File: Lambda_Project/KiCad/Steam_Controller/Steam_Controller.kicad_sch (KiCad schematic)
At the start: 156 parts, among them J1 MICROQTJ, P1 Conn_ARM_SWD_TagConnect_TC2030, P2 Conn_ARM_SWD_TagConnect_TC2030, P3 781271220, P4 781271220, Q10 DMN2300U-7, Q11 DMN2300U-7, Q12 DMP2035U-7, Q2 DMP2035U-7, Q3 MMBT3906, Q4 DMP2035U-7, Q5 DMP2035U-7, Q6 FDV304P, Q8 FDV304P, U1 LPC11U37FBD64/501,, U10 DMN63D8LDW-7, U2 TPD4E1U06DBVR - NG4P USB, U3 TPS61029DRCR, U4 TLV70230DBVT, U5 NRF51822-QFAB-T, U6 MPU6500, U7 A1304ELHLT-T, U8 A1304ELHLT-T, U9 DMN63D8LDW-7, X1 ABM8G-12.000MHZ-18-D2Y-T, X2 NX2520SA-16MHZ-STD-CSW-5

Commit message: Updated TODO in Schematic
Added a new TODO objective in the schematic as a test for the discord bot
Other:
- note added: "TODO: While tracing, keep an eye on the schematic and make sure it is correctt"
- note removed: "TODO: Sanity Check, reference datasheets, measure unsure values again."
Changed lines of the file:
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@@
 		)
 	)
-	(text "TODO: Sanity Check, reference datasheets, measure unsure values again."
+	(text "TODO: While tracing, keep an eye on the schematic and make sure it is correctt"
 		(exclude_from_sim no)
 		(at 513.334 51.562 0)
@@
 	)
 	(label "Inductor & Capacitor values taken from datasheet. These need to be high tolerance, within 1%"
-		(at 116.84 218.44 0)
+		(at 116.84 217.17 0)
 		(effects
 			(font

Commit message: V0.99 Update
Added trace updates from RoyMeetsWorld. Updated README. Added new images. Cleaned up some of the schematic and pcb.
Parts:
- added TP1, TP10, TP11, TP12, TP13, TP14, TP15, TP16, TP17, TP18, TP19, TP2, TP20, TP21, TP22, TP23, TP24, TP25, TP26, TP27, TP28, TP29, TP3, TP30, TP31, TP32, TP33, TP34, TP35, TP36, TP37, TP38, TP39, TP4, TP40, TP41, TP42, TP43, TP44, TP45, TP46, TP47, TP48, TP49, TP5, TP50, TP51, TP52, TP6, TP7, TP8, TP9: TestPoint, Steam_Controller:Steam Controller Test Pad, symbol Connector:TestPoint
- X1: value ABM8G-12.000MHZ-18-D2Y-T -> ABM8-12.000MHZ-B2-T
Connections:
- net A: now also TP17.1
- net ATP6 Left Signal: now also TP43.1
- net ATP6 Right Signal: now also TP8.1
- net B: now also TP12.1
- net D+: no longer J1.3 (D+)
- net D-: no longer J1.2 (D-)
- net FL: now also TP46.1
- net FR: now also TP51.1
- net GND: now also E1.1 (ANT1), TP10.1, TP24.1, TP48.1; no longer E1.2 (ANT2)
- net HALLTRIG1: now also TP31.1
- net HALLTRIG2: now also TP5.1
- net JOYBTN: now also TP26.1
- net JOYX: now also TP40.1
- net JOYY: now also TP41.1
- net LB: now also TP32.1
- net LED: now also TP47.1
- net LED Cathode: now also TP45.1
- net LT: now also TP30.1
- net RB: now also TP4.1
- net RT: now also TP6.1
- net S14: now also TP27.1
- net S16: now also TP11.1
- net S5: now also TP7.1
- net STEAM: now also TP36.1
- net U1-62: now also TP42.1
- net VBUS: now also TP1.1
- net VDD: now also TP23.1, TP28.1
- net X: now also TP16.1
- net Y: now also TP18.1
- net Net-(U1-PIO1_8): now reaches R39.2, R45.2, U1.36 (PIO0_8)
- net Net-(U1-PIO1_8): now also TP39.1
- net Net-(LED-C): now reaches LED1.1 (C), R1.1
- net Net-(LED-C): now also TP44.1
- net Net-(Bat1-Pos): now reaches BAT1.1 (pos), C57.1, D1.2 (A), D6.1 (K), Q4.2 (S)
- net Net-(Bat1-Pos): now also TP52.1
- net D+ USB: now reaches R14.1, R15.1, U2.1 (D1+)
- net D+ USB: now also J1.3 (D+), TP2.1
- net D3-K: now reaches C20.1, C22.2, C46.2, D3.1 (K), L1.1, Q12.2 (S), U3.1 (EN), U3.6 (VBAT)
- net D3-K: now also TP29.1
- net Net-(U1-PIO0_5): now reaches R7.2, U1.21 (PIO0_5), U6.24 (SDA/SDI)
- net Net-(U1-PIO0_5): now also TP35.1
- net Net-(U1-PIO1_17): now reaches U1.23 (PIO1_17), U5.20 (P0.14)
- net Net-(U1-PIO1_17): now also TP19.1
- net Net-(U1-PIO1_18): now reaches U1.28 (PIO1_18), U5.21 (P0.15)
- net Net-(U1-PIO1_18): now also TP20.1
- net Net-(U1-PIO1_9): now reaches R40.2, R46.1, U1.37 (PIO0_9)
- net Net-(U1-PIO1_9): now also TP38.1
- net P1-RESET: now reaches P1.3 (~{RESET}), R23.1
- net P1-RESET: now also TP15.1
- net Net-(U1-PIO1_29): now reaches R37.2, R41.1, U1.41 (PIO1_29)
- net Net-(U1-PIO1_29): now also TP37.1
- net P3-SS: now reaches P3.10 (SS), U1.64 (PIO1_6)
- net P3-SS: now also TP21.1
- net P3-ATP4: now reaches P3.5 (GND/ATP4)
- net P3-ATP4: now also TP25.1
- net P3-DR: now reaches P3.9 (DR), U1.63 (PIO1_16)
- net P3-DR: now also TP22.1
- net at C50.1, R44.2: now also E1.2 (ANT2); no longer E1.1 (ANT1)
- net Net-(U1-PIO0_4): now reaches R6.2, U1.20 (PIO0_4), U6.23 (SCL/SCLK)
- net Net-(U1-PIO0_4): now also TP34.1
- net Net-(U1-PIO1_23): now reaches U1.24 (PIO1_23), U6.12 (INT)
- net Net-(U1-PIO1_23): now also TP33.1
- net Net-(U1-PIO1_7): now reaches U1.30 (PIO0_7)
- net Net-(U1-PIO1_7): now also TP49.1
- net Net-(U1-PIO1_28): now reaches U1.31 (PIO1_28)
- net Net-(U1-PIO1_28): now also TP50.1
- net P4-DR: now reaches P4.9 (DR), U1.56 (PIO0_23)
- net P4-DR: now also TP13.1
- net P4-SS: now reaches P4.10 (SS), U1.57 (PIO1_15)
- net P4-SS: now also TP14.1
- net D- USB: now reaches R16.2, U2.6 (D1-)
- net D- USB: now also J1.2 (D-), TP3.1
- net P4-ATP4: now reaches P4.5 (GND/ATP4)
- net P4-ATP4: now also TP9.1
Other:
- note removed: "Front Left"
- note removed: "TODO: While tracing, keep an eye on the schematic and make sure it is correctt"
- moved on the sheet: E1

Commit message: Replaced MCU-6500 with BMI270 dual gyro
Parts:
- removed C35: 100nF, Capacitor_SMD:C_0201_0603Metric, symbol Device:C
- removed R6, R7: 4.7kΩ, Resistor_SMD:R_0201_0603Metric, symbol Device:R_US
- removed U6: MPU6500, Steam_Controller:QFN-24_L3.0-W3.0-P0.40-BL-EP, symbol Steam_Controller_Symbols:MPU6500
- added C21: 10nF, Capacitor_SMD:C_0201_0603Metric, symbol Device:C
- added C31, C7: 100nF, Capacitor_SMD:C_0201_0603Metric, symbol Device:C
- added R2, R5: 4.7kΩ, Resistor_SMD:R_0201_0603Metric, symbol Device:R_US
- added U11, U6: BMI270, Steam_Controller:XDCR_BMI270, symbol Steam_Controller_Symbols:BMI270
- C37: value 10nF -> 100nF
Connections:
- net Net-(U1-PIO1_23) is gone; now on net Net-(U1-PIO1_17): TP33.1, U1.24 (PIO1_23)
- net Net-(U1-PIO1_9) is gone; now on net Net-(U1-PIO1_8): R40.2, R46.1, TP38.1, U1.37 (PIO0_9)
- net GND: now also C36.1, C37.1, C21.2, C31.1, C7.1, U11.6 (GNDIO), U11.7 (GND), U6.1 (SDO), U6.6 (GNDIO), U6.7 (GND); no longer C36.2, C37.2
- net Net-(U1-PIO0_4): now also R2.1, U11.13 (SCX), U6.13 (SCX)
- net Net-(U1-PIO0_5): now also R5.1, U11.14 (SDX), U6.14 (SDX)
- net Net-(U1-PIO1_17): now also U11.4 (INT1)
- net VDD: now also C36.2, C37.2, C21.1, C31.2, C7.2, R2.2, R5.2, U11.1 (SDO), U11.5 (VDDIO), U11.8 (VDD), U6.5 (VDDIO), U6.8 (VDD); no longer C37.1
- net at U1.53 (PIO0_16): now also U6.4 (INT1)

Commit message: Fix overlapping routing of INT trace to U11
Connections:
- net Net-(U1-PIO1_17): no longer TP33.1, U1.24 (PIO1_23), U11.4 (INT1)
- new net Net-(U1-PIO1_23): TP33.1, U1.24 (PIO1_23), U11.4 (INT1)
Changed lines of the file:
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@@
 	)
 	(junction
-		(at 205.74 185.42)
-		(diameter 0)
-		(color 0 0 0 0)
-	)
-	(junction
 		(at 353.06 23.368)
 		(diameter 0)
@@
 	)
 	(junction
+		(at 269.24 158.75)
+		(diameter 0)
+		(color 0 0 0 0)
+	)
+	(junction
 		(at 307.34 10.16)
 		(diameter 0)
@@
 	)
 	(junction
-		(at 262.89 185.42)
-		(diameter 0)
-		(color 0 0 0 0)
-	)
-	(junction
 		(at 293.37 332.74)
 		(diameter 0)
@@
 	(wire
 		(pts
-			(xy 262.89 185.42) (xy 497.84 185.42)
-		)
-		(stroke
-			(width 0)
-			(type default)
-		)
-	)
-	(wire
-		(pts
 			(xy 375.92 25.908) (xy 375.92 27.94)
 		)
@@
 	(wire
 		(pts
-			(xy 205.74 158.75) (xy 279.4 158.75)
-		)
-		(stroke
-			(width 0)
-			(type default)
-		)
-	)
-	(wire
-		(pts
 			(xy 267.97 335.28) (xy 267.97 342.9)
 		)
@@
 	(wire
 		(pts
-			(xy 262.89 185.42) (xy 205.74 185.42)
+			(xy 66.04 185.42) (xy 262.89 185.42)
 		)
 		(stroke
@@
 	(wire
 		(pts
+			(xy 260.35 158.75) (xy 269.24 158.75)
+		)
+		(stroke
+			(width 0)
+			(type default)
+		)
+	)
+	(wire
+		(pts
 			(xy 123.19 142.24) (xy 123.19 110.49)
 		)
@@
 	(wire
 		(pts
+			(xy 269.24 185.42) (xy 497.84 185.42)
+		)
+		(stroke
+			(width 0)
+			(type default)
+		)
+	)
+	(wire
+		(pts
 			(xy 233.68 394.97) (xy 247.65 394.97)
 		)
@@
 	(wire
 		(pts
+			(xy 269.24 158.75) (xy 279.4 158.75)
+		)
+		(stroke
+			(width 0)
+			(type default)
+		)
+	)
+	(wire
+		(pts
 			(xy 347.98 120.65) (xy 342.9 120.65)
 		)
@@
 	(wire
 		(pts
+			(xy 269.24 158.75) (xy 269.24 185.42)
+		)
+		(stroke
+			(width 0)
+			(type default)
+		)
+	)
+	(wire
+		(pts
 			(xy 72.39 168.91) (xy 67.31 168.91)
 		)
@@
 	(wire
 		(pts
-			(xy 205.74 158.75) (xy 205.74 185.42)
-		)
-		(stroke
-			(width 0)
-			(type default)
-		)
-	)
-	(wire
-		(pts
 			(xy 535.94 143.51) (xy 544.83 143.51)
 		)
@@
 		)
 		(stroke
-			(width 0)
-			(type default)
-		)
-	)
-	(wire
-		(pts
-			(xy 205.74 185.42) (xy 66.04 185.42)
-		)
-		(stroke

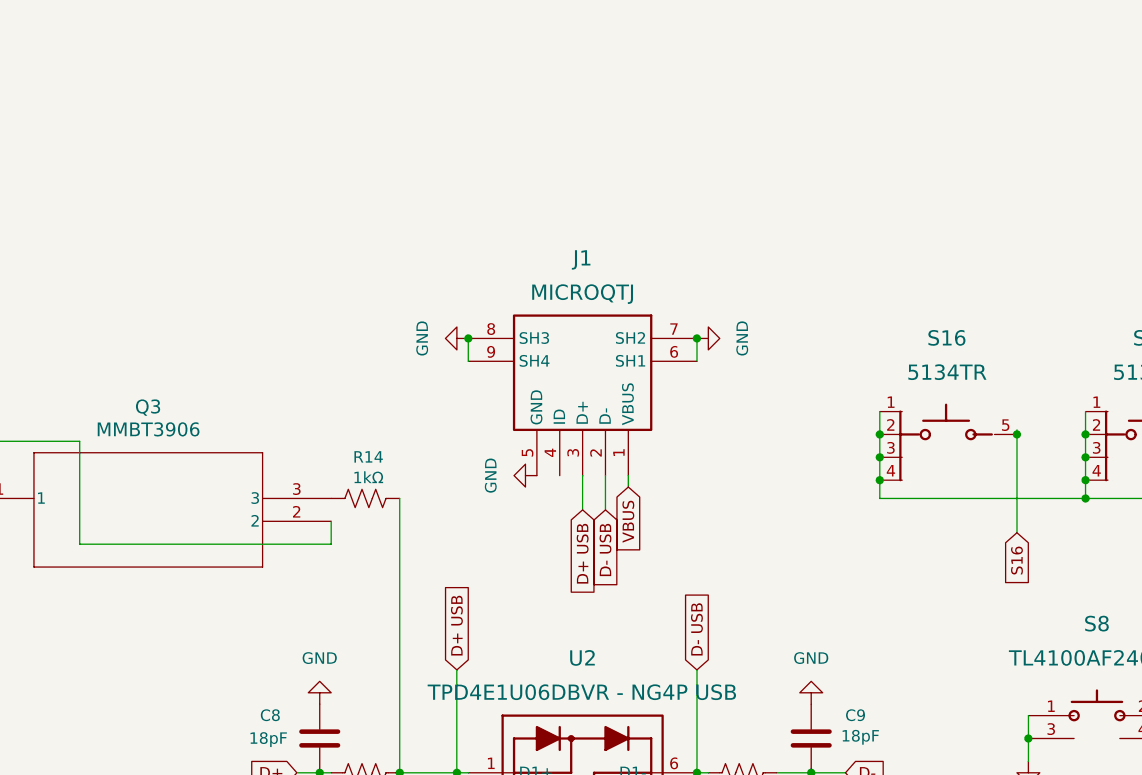
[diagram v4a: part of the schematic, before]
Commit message: Replaced MicroUSB with USB-C
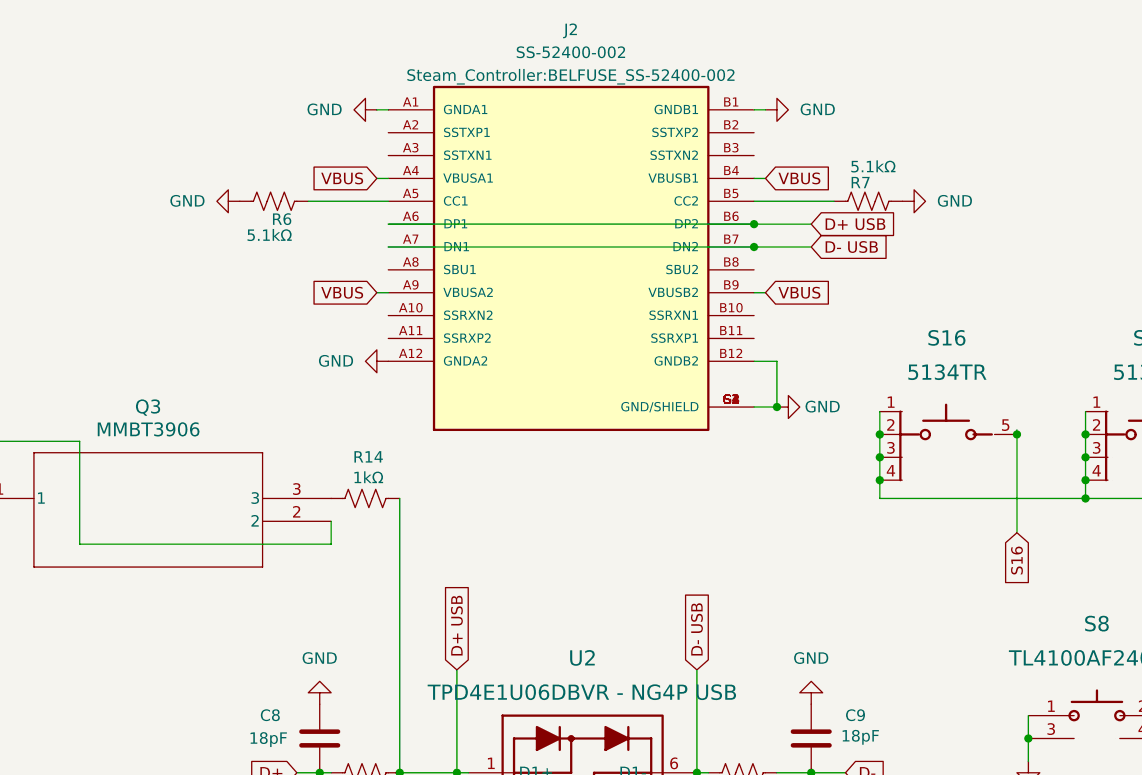
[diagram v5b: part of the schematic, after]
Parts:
- removed J1: MICROQTJ, Steam_Controller:MICRO-USB-SMD_MICROQTJ-5P, symbol Steam_Controller_Symbols:MICROQTJ
- added J2: SS-52400-002, Steam_Controller:BELFUSE_SS-52400-002, symbol Steam_Controller_Symbols:SS-52400-002
- added R6, R7: 5.1kΩ, Resistor_SMD:R_0201_0603Metric, symbol Device:R_US
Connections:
- net D+ USB: now also J2.A6 (DP1), J2.B6 (DP2)
- net D- USB: now also J2.A7 (DN1), J2.B7 (DN2)
- net GND: now also J2.A1 (GNDA1), J2.A12 (GNDA2), J2.B1 (GNDB1), J2.B12 (GNDB2), J2.G1 (GND/SHIELD), J2.G2 (GND/SHIELD), J2.G3 (GND/SHIELD), J2.G4 (GND/SHIELD), J2.S1 (GND/SHIELD), J2.S2 (GND/SHIELD), J2.S3 (GND/SHIELD), J2.S4 (GND/SHIELD), R6.2, R7.2
- net VBUS: now also J2.A4 (VBUSA1), J2.A9 (VBUSA2), J2.B4 (VBUSB1), J2.B9 (VBUSB2)
- new net: J2.A5 (CC1), R6.1
- new net: J2.B5 (CC2), R7.1

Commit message: ECAD: Insert ESP32-S3, Delete Unnecessary Stuff, Organize
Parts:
- removed C10, C11: C0402C180J3GACAUTO, Capacitor_SMD:C_0201_0603Metric, symbol Steam_Controller_Symbols:C0402C180J3GACAUTO
- removed C23, C24: C0402C120F5GACTU, Capacitor_SMD:C_0201_0603Metric, symbol Steam_Controller_Symbols:C0402C120F5GACTU
- removed C25, C28, C34: 100nF, Capacitor_SMD:C_0201_0603Metric, symbol Device:C
- removed C26: 1nF, Capacitor_SMD:C_0201_0603Metric, symbol Device:C
- removed C27: 2.2pF, Capacitor_SMD:C_0201_0603Metric, symbol Device:C
- removed C29: 1pF, Capacitor_SMD:C_0201_0603Metric, symbol Device:C
- removed C30: 1.5pF, Capacitor_SMD:C_0201_0603Metric, symbol Device:C
- removed C32: 47nF, Capacitor_SMD:C_0201_0603Metric, symbol Device:C
- removed C33: 2.2nF, Capacitor_SMD:C_0201_0603Metric, symbol Device:C
- removed C50: 1.87 pF, Capacitor_SMD:C_0201_0603Metric, symbol Device:C
- removed E1: Antenna, Steam_Controller:Antenna_footprint, symbol Steam_Controller_Symbols:Antenna
- removed L2: 3.3nH, Inductor_SMD:L_0201_0603Metric, symbol Device:L
- removed L3: 4.7nH, Inductor_SMD:L_0201_0603Metric, symbol Device:L
- removed L5: 10nH, Inductor_SMD:L_0201_0603Metric, symbol Device:L
- removed P2: Conn_ARM_SWD_TagConnect_TC2030, Connector:Tag-Connect_TC2030-IDC-FP_2x03_P1.27mm_Vertical, symbol Connector:Conn_ARM_SWD_TagConnect_TC2030
- removed R21, R44: 50mΩ, Resistor_SMD:R_0201_0603Metric, symbol Device:R_US
- removed U5: NRF51822-QFAB-T, Steam_Controller:QFN-48_L6.0-W6.0-P0.40-TL-EP4.6, symbol Steam_Controller_Symbols:NRF51822-QFAB-T
- removed X1: ABM8-12.000MHZ-B2-T, Steam_Controller:XTAL_ABM8-12.000MHZ-B2-T, symbol Steam_Controller_Symbols:ABM8-12.000MHZ-B2-T
- removed X2: NX2520SA-16MHZ-STD-CSW-5, Steam_Controller:NX2520SA16MHZSTDCSW5, symbol Steam_Controller_Symbols:NX2520SA-16MHZ-STD-CSW-5
- added U12: ESP32-S3, Steam_Controller:ESP32-S3, symbol Steam_Controller_Symbols:ESP32-S3
- S10: value TL4100AF240QG -> Right Bumper
- S14: value 5134TR -> Right Paddle
- S16: value 5134TR -> Left Paddle
- S2: value 5134TR -> Right Pad Click
- S3: value SKRRAAE010 -> Left Trigger
- S5: value 5134TR -> Left Pad Click
- S6: value SKRRAAE010 -> Right Trigger
- S8: value TL4100AF240QG -> Left Bumper
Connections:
- net GND: now also JY1.A11; no longer JY1.A13
- net Net-(U1-PIO1_18): no longer U1.28 (PIO1_18)
- net Net-(U1-PIO1_8): no longer R40.2, R46.1, TP38.1, U1.37 (PIO0_9)
- net U1-62: now also JY1.A13; no longer JY1.A11
- net Net-(U1-PIO0_5) renamed GYRO-DAT
- net Net-(U1-PIO1_23) renamed GYRO-INT
- net S14 renamed RPADDLE
- net S16 renamed LPADDLE
- net S2 renamed RPADCLICK
- net S5 renamed LPADCLICK
- new net: U12.2 (VDD3P3), U12.3 (VDD3P3)
- new net Net-(U1-PIO1_9): R40.2, R46.1, TP38.1, U1.37 (PIO0_9)
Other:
- note removed: "C31 after R44 to GND - Unpopulated"
- note removed: "R20 to GND - Unpopulated"
